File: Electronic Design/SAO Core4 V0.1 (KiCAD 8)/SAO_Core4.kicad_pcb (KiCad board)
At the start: 2 copper layers, 50.8 x 63.5 mm, 102 parts, among them Q1 MMBT4403LT1G, Q13 MMBT4403LT1G, Q14 MMBT4401LT1G, Q17 MMBT4403LT1G, Q18 MMBT4401LT1G, Q2 MMBT4401LT1G, Q22 SL3401A, Q3 MMBT4403LT1G, Q4 MMBT4401LT1G, Q5 MMBT4403LT1G, Q6 MMBT4401LT1G, Q7 Q_NMOS_DGS_AO3400A, U1 MCP23017_SS, U10 SN74HC02DR, U7 SSP9193-33M5R, U9 LM393, X1 SAO_conn_SFH11-NBPC-D03-ST-BK, X2 SAO_conn_SFH11-NBPC-D03-ST-BK, X9 QWIIC

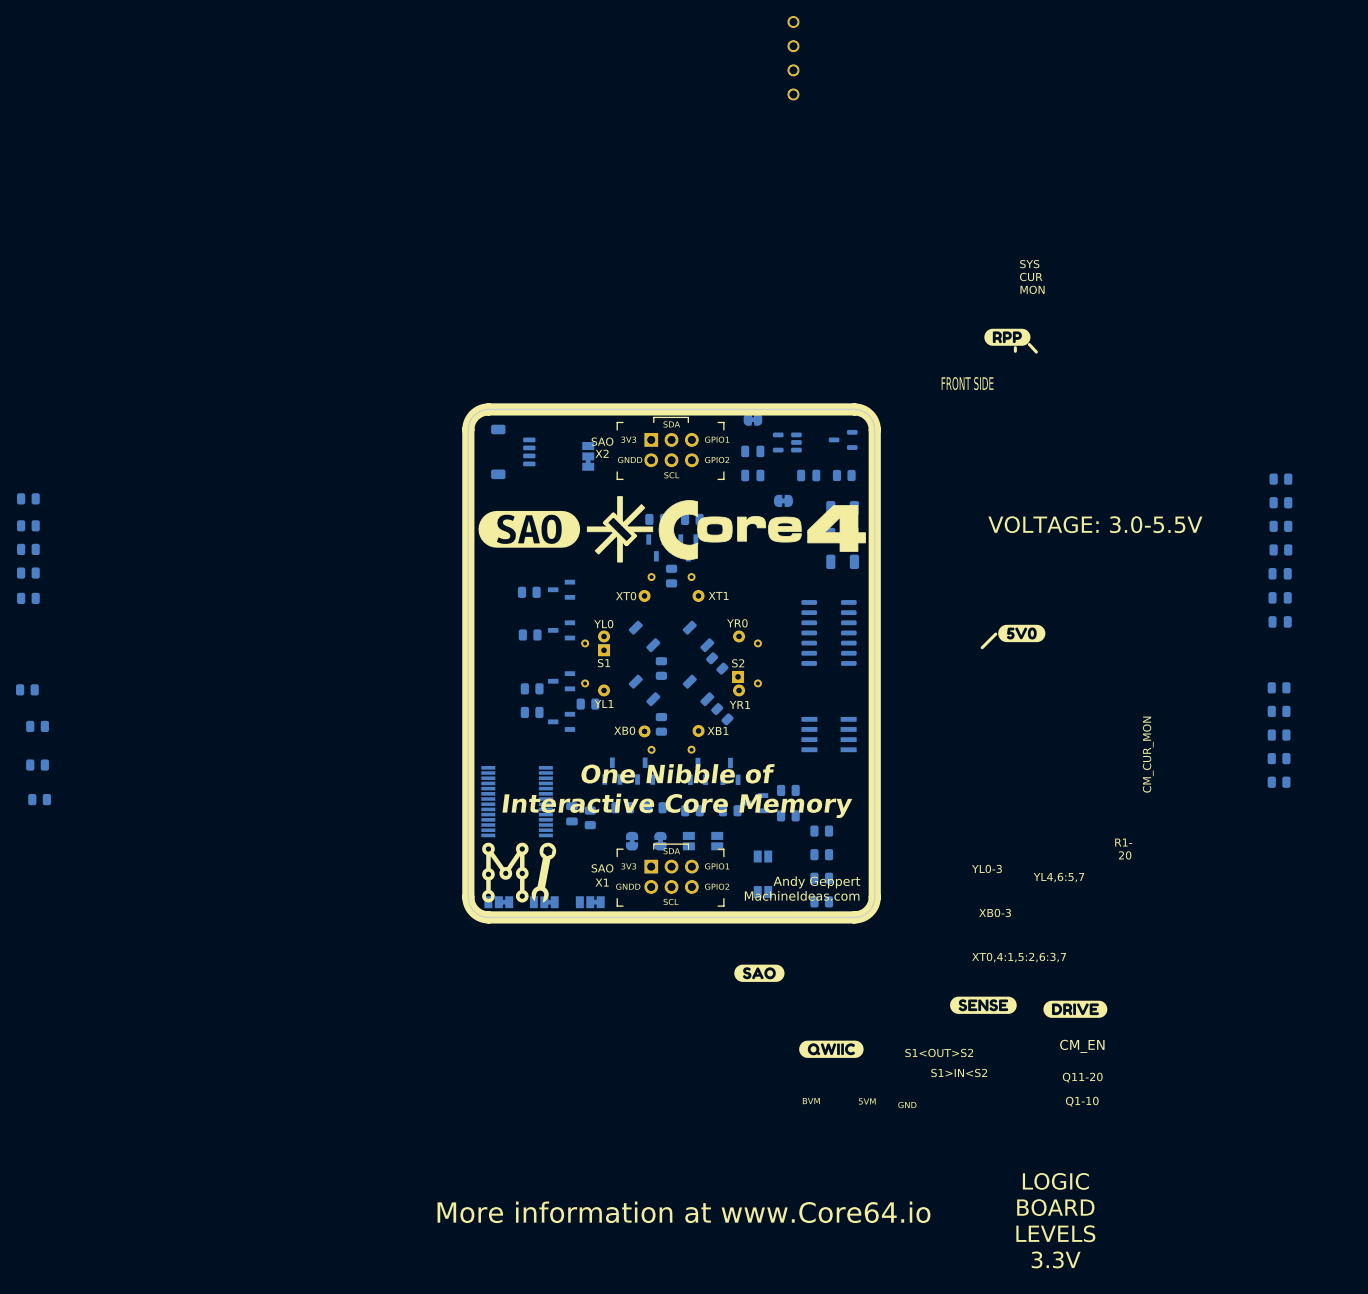
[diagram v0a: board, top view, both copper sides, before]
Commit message: Refine
Cleanup schematic, plan drive scheme, commit to CM_EN, spare IO.
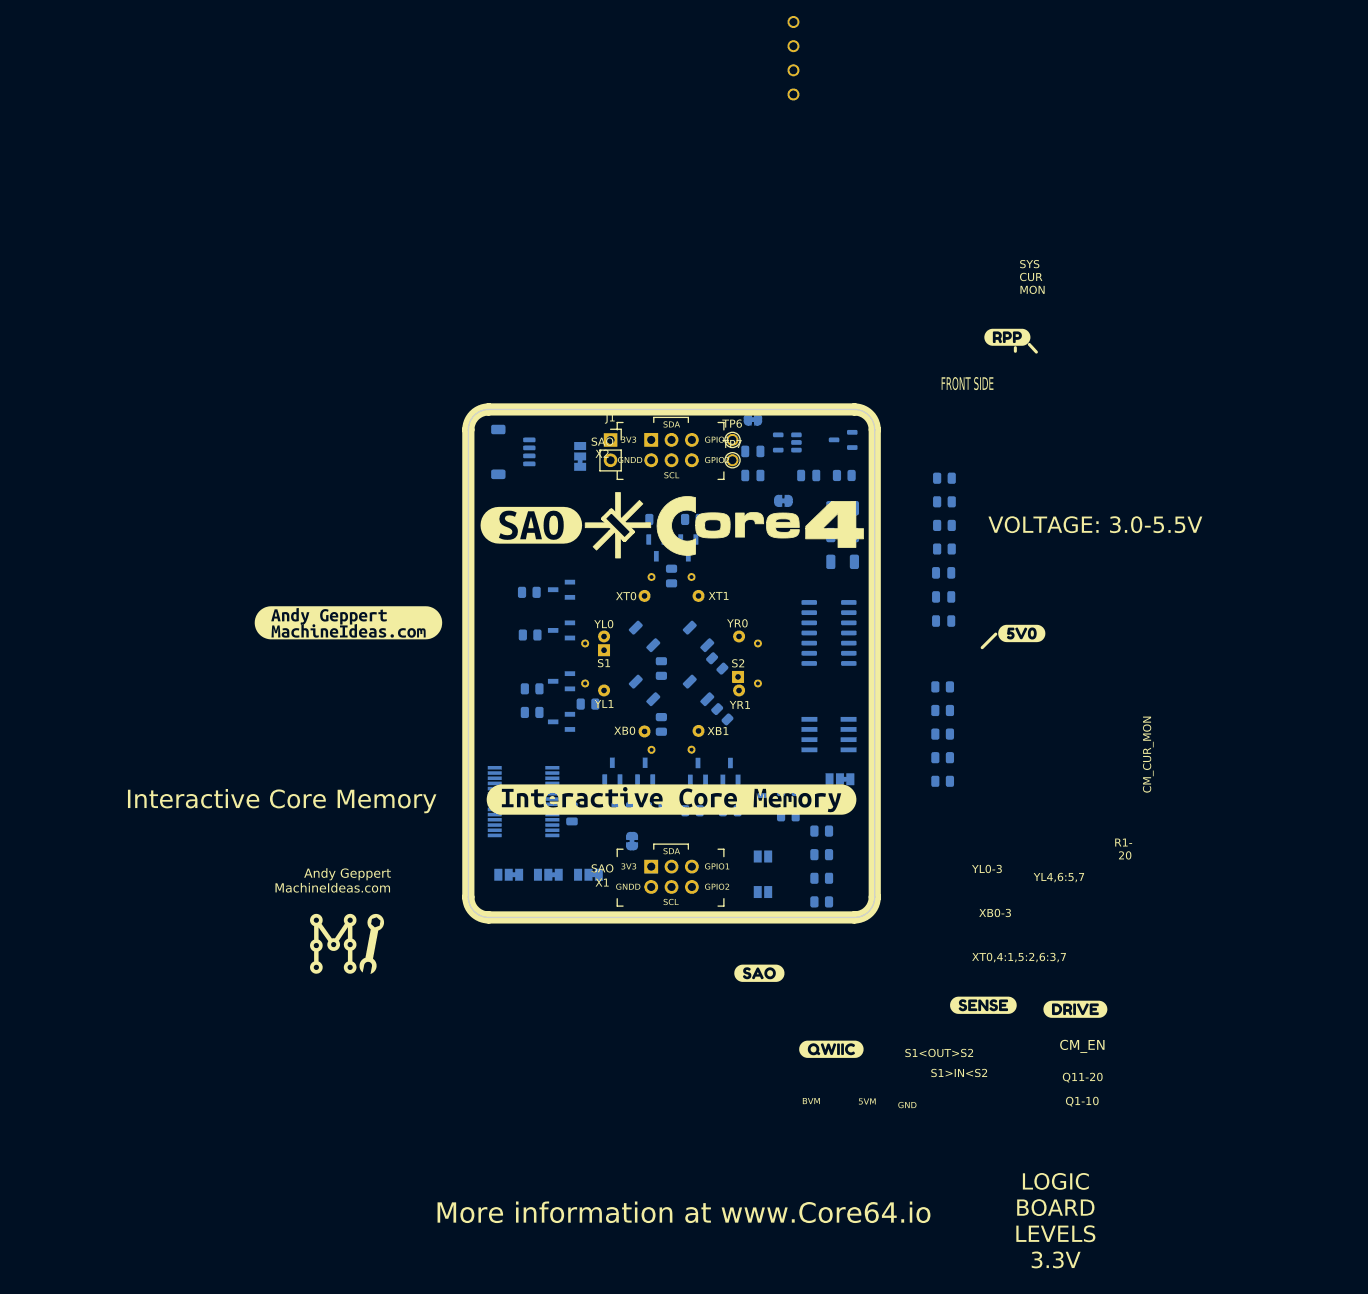
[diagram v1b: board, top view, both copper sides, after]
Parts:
- removed JP3: CME_BYPASS, Jumper:SolderJumper-2_P1.3mm_Bridged_RoundedPad1.0x1.5mm
- removed JP5: EN_LED1, Jumper:SolderJumper-2_P1.3mm_Open_Pad1.0x1.5mm
- removed JP6: EN_GPIO1, Jumper:SolderJumper-2_P1.3mm_Open_Pad1.0x1.5mm
- removed R11, R12, R15, R16, R19, R20, R22, R23, R24, R26: 10K, Resistor_SMD:R_0805_2012Metric
- added J1: ALT. BATT., Connector_PinSocket_2.54mm:PinSocket_1x02_P2.54mm_Vertical, F.Cu at (99.9, 97.9)
- added JP11: CM_SNS_SEL, Jumper:SolderJumper-3_P1.3mm_Bridged12_Pad1.0x1.5mm, B.Cu at (128.6, 140.3)
- added TP6: GPB6, Andy_Footprint_Library:TestPoint_THTPad_D1.5mm_Drill1.0mm, F.Cu at (115.1, 97.9)
- added TP7: GPB7, Andy_Footprint_Library:TestPoint_THTPad_D1.5mm_Drill1.0mm, F.Cu at (115.1, 100.4)
- added kibuzzard-66BD76FA: G***, kibuzzard-66BD76FA, F.Cu at (107.5, 142.9)
- added kibuzzard-66BD78BD: G***, kibuzzard-66BD78BD, F.Cu at (67.1, 120.8)
- moved R47 42.1 mm to (141.6, 102.7)
- moved R48 42.1 mm to (141.6, 105.6)
- moved R49 42.1 mm to (141.6, 108.6)
- moved R50 42.1 mm to (141.6, 111.5)
- moved R51 42.1 mm to (141.4, 128.8)
- moved R52 42.1 mm to (141.4, 131.7)
- moved R53 42.1 mm to (141.4, 134.7)
- moved R54 42.1 mm to (141.4, 137.6)
- moved R55 42.1 mm to (141.4, 140.6)
- moved C17 42.1 mm to (141.5, 114.5)
- moved C18 42.1 mm to (141.5, 117.5)
- moved C19 42.1 mm to (141.5, 120.5)
- moved L2 23.3 mm to (67.4, 161.2)
- moved JP7 3.65 mm to (87.2, 152.3)
- moved JP8 3.47 mm to (92.1, 152.3)
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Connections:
- net /CM_SENSE_RESET renamed /CM_SNS_RST
- R13 pad 2: /CM_Q7P -> /CM_Q7P_9N
- R14 pad 2: /CM_Q7N -> /CM_Q7N_9P
- R17 pad 2: /CM_Q9P -> /CM_Q7N_9P
- R18 pad 2: /CM_Q9N -> /CM_Q7P_9N
- U1 pad 1: /CM_Q7N -> /CM_Q7N_9P
- U1 pad 2: /CM_Q7P -> /CM_Q7P_9N
- U1 pad 27: /CM_SENSE_PULSE -> /CM_EN
- U1 pad 3: /CM_Q9N -> /LED_1
- U1 pad 4: /CM_Q9P -> /LED_2
- U1 pad 5: /LED_1 -> /LED_3
- U1 pad 6: /LED_2 -> /LED_4
- U1 pad 7: /LED_3 -> /SPARE_GPB6
- U1 pad 8: /LED_4 -> /SPARE_GPB7
- U10 pad 10: /CM_SENSE_PULSE -> /CM_SNS_PLS
- U10 pad 11: /CM_SENSE_PULSE -> /CM_SNS_PLS
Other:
- board text added: "Interactive Core Memory"
- board text removed: "One Nibble of Interactive Core Memory"

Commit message: Refine schematic
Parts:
- removed J1: ALT. BATT., Connector_PinSocket_2.54mm:PinSocket_1x02_P2.54mm_Vertical
- removed JP18: CM_CUR_MON, Jumper:SolderJumper-2_P1.3mm_Bridged_RoundedPad1.0x1.5mm
- removed kibuzzard-64179E5D: G***, kibuzzard-64179E5D
- removed kibuzzard-66BD76FA: G***, kibuzzard-66BD76FA
- added kibuzzard-66C119C9: G***, kibuzzard-66C119C9, F.Cu at (107.5, 142.9)
- R44: renamed from R33; value 10K -> 4K7
- R60: renamed from R7; value 470 -> 120
- R61: renamed from R8; value 470 -> 120
- R62: renamed from R9; value 470 -> 120
- R63: renamed from R10; value 470 -> 120
- kibuzzard-64179D69: moved to B.Cu
- moved X9 66.5 mm to (128.1, 152.3), turned to -90 degrees
- moved R28 56.1 mm to (86.9, 101.2), turned to 0 degrees
- moved JP22 54.3 mm to (121.4, 148.0)
- moved TP6 53.4 mm to (117.7, 151.2)
- moved TP7 53.4 mm to (117.7, 153.8)
- moved C17 51.0 mm to (191.1, 126.7)
- moved C18 51.0 mm to (191.1, 129.7)
- moved C19 51.0 mm to (191.1, 132.7)
- moved R47 51.0 mm to (191.2, 114.9)
- moved R48 51.0 mm to (191.2, 117.8)
- moved R49 51.0 mm to (191.2, 120.8)
- moved R50 51.0 mm to (191.2, 123.7)
- moved R51 51.0 mm to (190.9, 141.0)
- moved R52 51.0 mm to (190.9, 143.9)
- moved R53 51.0 mm to (190.9, 146.9)
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- renumbered JP11 to JP21, JP10 to JP22, JP2 to JP23, JP4 to JP24, JP1 to JP3, JP7 to JP30, JP8 to JP31, JP9 to JP32, Q7 to Q21, R28 to R27, R27 to R28, R31 to R30, R32 to R31, R29 to R32, R30 to R33, U1 to U11
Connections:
- net /CM_Q1N renamed /CMDQ1N
- net /CM_Q1P renamed /CMDQ1P
- net /CM_Q2N renamed /CMDQ2N
- net /CM_Q2P renamed /CMDQ2P
- net /CM_Q3N renamed /CMDQ3N
- net /CM_Q3P renamed /CMDQ3P
- net /CM_Q7N_9P renamed /CMDQ7N9P
- net /CM_Q7P_9N renamed /CMDQ7P9N
- JP22 pad 1: VIN -> 3V3
- JP22 pad 3: 3V3 -> VIN
- Q1 pad 2: VMEM -> 3V3
- Q13 pad 2: VMEM -> 3V3
- Q17 pad 2: VMEM -> 3V3
- Q3 pad 2: VMEM -> 3V3
- Q5 pad 2: VMEM -> 3V3
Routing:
- net 3V3: track 0.00 -> 215.2 mm, vias 0 -> 4
- net VIN: track 0.00 -> 126.3 mm
- net /GPIO1: track 0.00 -> 125.3 mm
- net /GPIO2: track 0.00 -> 121.3 mm
- net /SDA: track 0.00 -> 117.3 mm
- net /SCL: track 0.00 -> 113.3 mm
- net GND: track 0.00 -> 106.9 mm
- net GMEM: track 0.00 -> 53.4 mm, vias 0 -> 1
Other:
- board text added: "+A2+A1+A0"
- board text added: "www.Core64.io Andy Geppert"
- board text removed: "5V0_CUR_MON"
- board text removed: "Andy Geppert MachineIdeas.com"
